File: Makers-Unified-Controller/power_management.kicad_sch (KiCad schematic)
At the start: 16 parts, among them J3 BAT Connector, Q1 PJA3401A_R1_00001, SW1 SW_DPDT_x2, U6 TPS62046DRCR

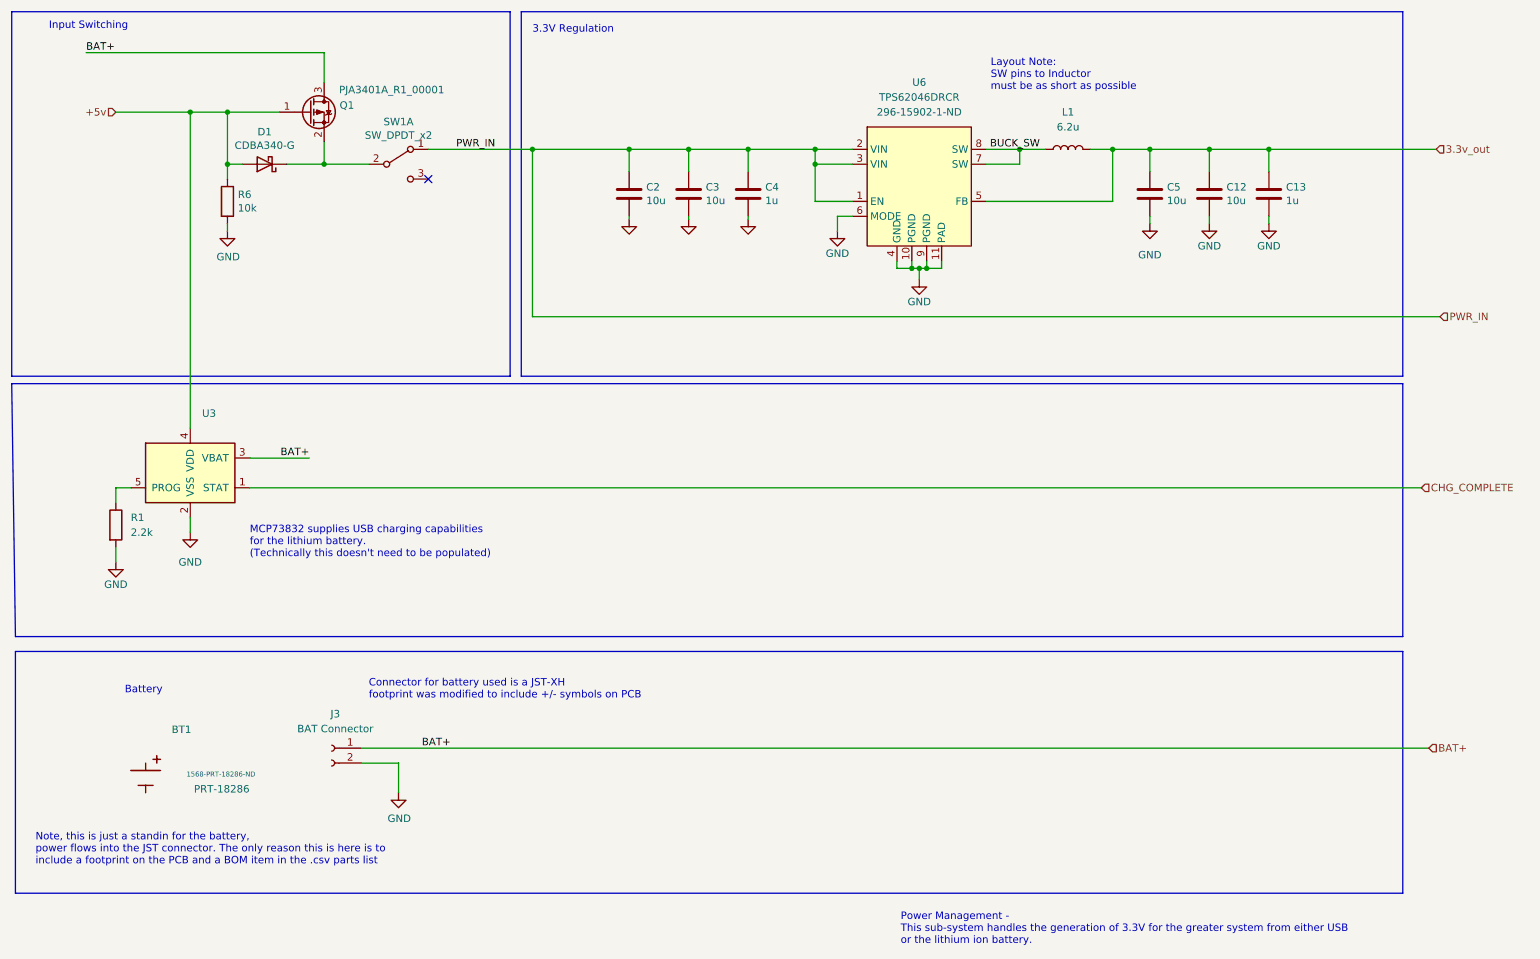
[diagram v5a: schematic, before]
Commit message: minor edits to schematic and Ibom
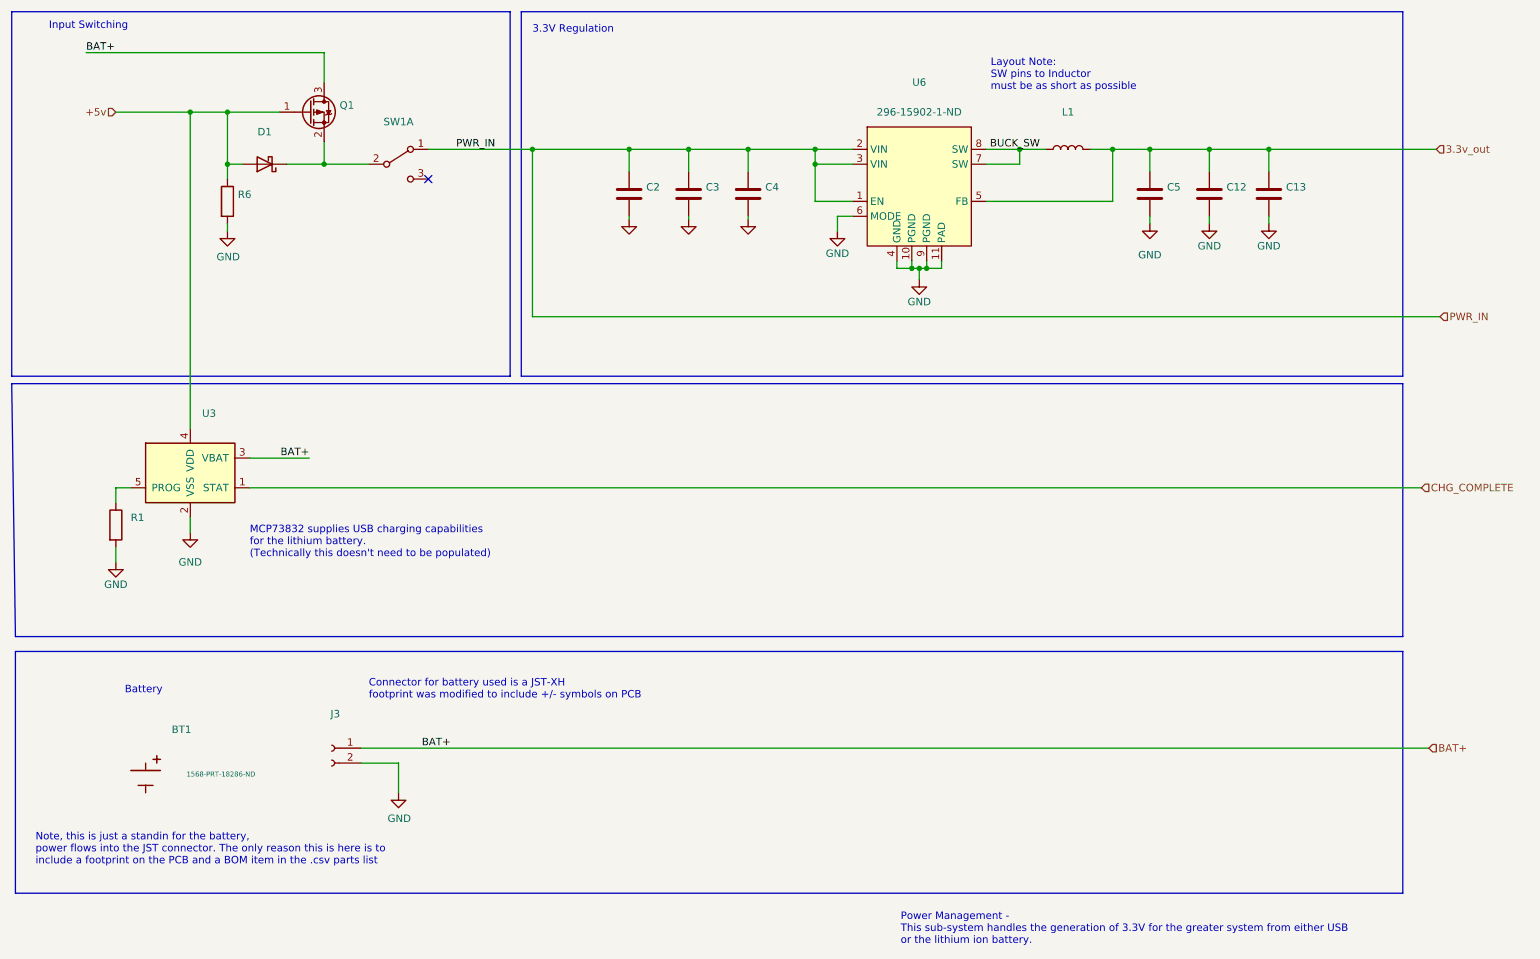
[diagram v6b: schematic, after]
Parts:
- BT1: value PRT-18286 -> (none)
- C12, C2, C3, C5: value 10u -> (none)
- C13, C4: value 1u -> (none)
- D1: value CDBA340-G -> (none)
- J3: value BAT Connector -> (none)
- L1: value 6.2u -> (none)
- Q1: value PJA3401A_R1_00001 -> (none)
- R1: value 2.2k -> (none); digikey_part_number RMCF0805JT2K20CT-ND -> RMCF0805FT4K70CT-ND
- R6: value 10k -> (none)
- SW1: value SW_DPDT_x2 -> (none)
- U6: value TPS62046DRCR -> (none)
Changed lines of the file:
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@@
       (effects (font (size 1.27 1.27)) (justify left))
     )
-    (property "Value" "10u" (id 1) (at 135.001 46.228 0)
+    (property "Value" "" (id 1) (at 135.001 46.228 0)
       (effects (font (size 1.27 1.27)) (justify left))
     )
@@
     (in_bom yes) (on_board yes)
     (property "Reference" "D1" (id 0) (at 69.85 34.4932 0))
-    (property "Value" "CDBA340-G" (id 1) (at 69.85 36.8046 0))
+    (property "Value" "" (id 1) (at 69.85 36.8046 0))
     (property "Footprint" "" (id 2) (at 69.85 40.005 0)
       (effects (font (size 1.27 1.27)) hide)
@@
       (effects (font (size 1.27 1.27)) (justify left))
     )
-    (property "Value" "10k" (id 1) (at 65.278 47.498 0)
+    (property "Value" "" (id 1) (at 65.278 47.498 0)
       (effects (font (size 1.27 1.27)) (justify left))
     )
@@
       (effects (font (size 1.27 1.27)) (justify left))
     )
-    (property "Value" "10u" (id 1) (at 234.061 46.228 0)
+    (property "Value" "" (id 1) (at 234.061 46.228 0)
       (effects (font (size 1.27 1.27)) (justify left))
     )
@@
       (effects (font (size 1.27 1.27)) (justify left))
     )
-    (property "Value" "1u" (id 1) (at 155.321 46.228 0)
+    (property "Value" "" (id 1) (at 155.321 46.228 0)
       (effects (font (size 1.27 1.27)) (justify left))
     )
@@
       (effects (font (size 1.27 1.27)) (justify left))
     )
-    (property "Value" "10u" (id 1) (at 223.901 46.228 0)
+    (property "Value" "" (id 1) (at 223.901 46.228 0)
       (effects (font (size 1.27 1.27)) (justify left))
     )
@@
       (effects (font (size 1.27 1.27)) (justify left))
     )
-    (property "Value" "1u" (id 1) (at 244.221 46.228 0)
+    (property "Value" "" (id 1) (at 244.221 46.228 0)
       (effects (font (size 1.27 1.27)) (justify left))
     )
@@
     (in_bom yes) (on_board yes) (fields_autoplaced)
     (property "Reference" "J3" (id 0) (at 81.915 133.858 0))
-    (property "Value" "BAT Connector" (id 1) (at 81.915 136.398 0))
+    (property "Value" "" (id 1) (at 81.915 136.398 0))
     (property "Footprint" "" (id 2) (at 81.28 139.7 0)
       (effects (font (size 1.27 1.27)) hide)
@@
       (effects (font (size 1.27 1.27)) (justify left))
     )
-    (property "Value" "10u" (id 1) (at 145.161 46.228 0)
+    (property "Value" "" (id 1) (at 145.161 46.228 0)
       (effects (font (size 1.27 1.27)) (justify left))
     )
@@
       (effects (font (size 1.27 1.27)) (justify left))
     )
-    (property "Value" "PRT-18286" (id 1) (at 57.785 146.685 90)
+    (property "Value" "" (id 1) (at 57.785 146.685 90)
       (effects (font (size 1.27 1.27)) (justify left))
     )
@@
       (effects (font (size 1.27 1.27)) (justify left))
     )
-    (property "Value" "2.2k" (id 1) (at 46.99 102.8699 0)
+    (property "Value" "" (id 1) (at 46.99 102.8699 0)
       (effects (font (size 1.27 1.27)) (justify left))
     )
@@
       (effects (font (size 1.27 1.27)) hide)
     )
-    (property "digikey_part_number" "RMCF0805JT2K20CT-ND" (id 4) (at 44.45 101.6 0)
+    (property "digikey_part_number" "RMCF0805FT4K70CT-ND" (id 4) (at 44.45 101.6 0)
       (effects (font (size 1.27 1.27)) hide)
     )
@@
       (effects (font (size 1.27 1.27)) (justify left))
     )
-    (property "Value" "PJA3401A_R1_00001" (id 1) (at 82.55 27.305 0)
+    (property "Value" "" (id 1) (at 82.55 27.305 0)
       (effects (font (size 1.27 1.27)) (justify left))
     )
@@
     (in_bom yes) (on_board yes)
     (property "Reference" "SW1" (id 0) (at 92.71 32.766 0))
-    (property "Value" "SW_DPDT_x2" (id 1) (at 92.71 35.0774 0))
+    (property "Value" "" (id 1) (at 92.71 35.0774 0))
     (property "Footprint" "" (id 2) (at 92.71 40.005 0)
       (effects (font (size 1.27 1.27)) hide)
@@
     (in_bom yes) (on_board yes) (fields_autoplaced)
     (property "Reference" "L1" (id 0) (at 207.01 31.115 90))
-    (property "Value" "6.2u" (id 1) (at 207.01 33.655 90))
+    (property "Value" "" (id 1) (at 207.01 33.655 90))
     (property "Footprint" "" (id 2) (at 207.01 37.465 0)
       (effects (font (size 1.27 1.27)) hide)
@@
     (in_bom yes) (on_board yes) (fields_autoplaced)
     (property "Reference" "U6" (id 0) (at 181.61 26.035 0))
-    (property "Value" "TPS62046DRCR" (id 1) (at 181.61 28.575 0))
+    (property "Value" "" (id 1) (at 181.61 28.575 0))
     (property "Footprint" "" (id 2) (at 146.05 15.875 0)
       (effects (font (size 1.27 1.27)) hide)
